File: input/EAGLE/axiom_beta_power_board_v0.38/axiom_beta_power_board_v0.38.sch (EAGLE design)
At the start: 328 parts, among them Q1 NX3008NBKT, U1 PIC16F15325-JQ, U10 AP7312-3333W6-7, U11 AP7312-3333W6-7, U12 AP7312-3333W6-7, U13 AP7312-3333W6-7, U14 PAC1720, U15 PAC1720, U16 PAC1720, U17 PAC1720, U18 PAC1720, U19 PAC1720, U2 TPS82130SIL-GM, U20 PAC1720, U21 PAC1720, U22 PAC1720, U23 PAC1720, U24 PAC1720, U25 PCA9306GM, U26 SC202A, U27 TS3A4751, U28 IP4251CZ16-8-TTL, U29 LM75BGD, U3 TPS82130SIL-GM, U30 PCA9306GM, U31 NCP715, U4 PCA9306GM, U5 PCA9306GM, U6 MCP23018-E/MJ, U7 MCP23018-E/MJ, U8 MCP23018-E/MJ, U9 MCP23018-E/MJ, X1 PICO-SPOX-5

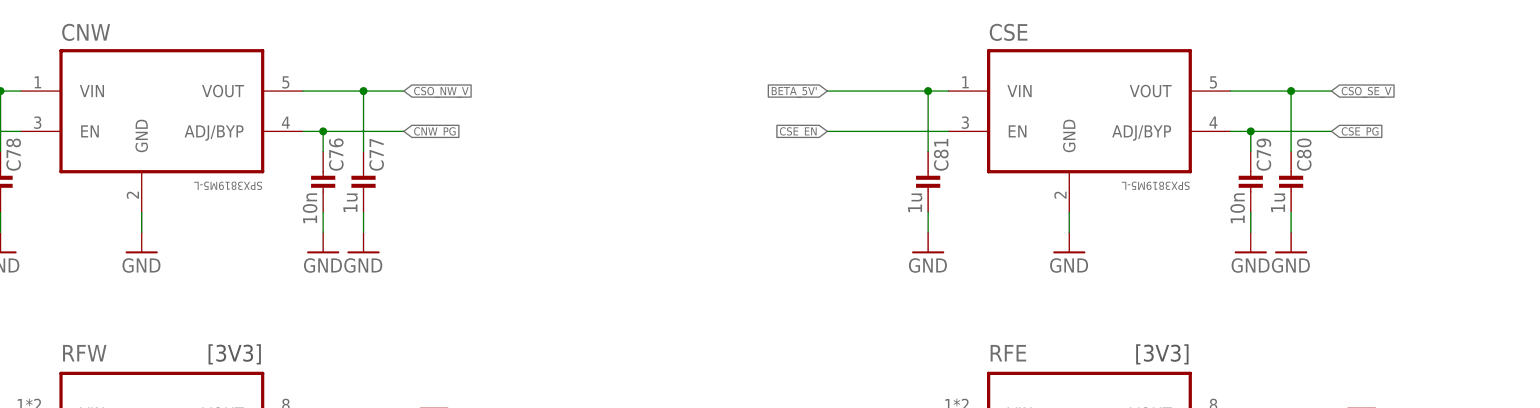
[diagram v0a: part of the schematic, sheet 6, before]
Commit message: MB & PB V0.38 added
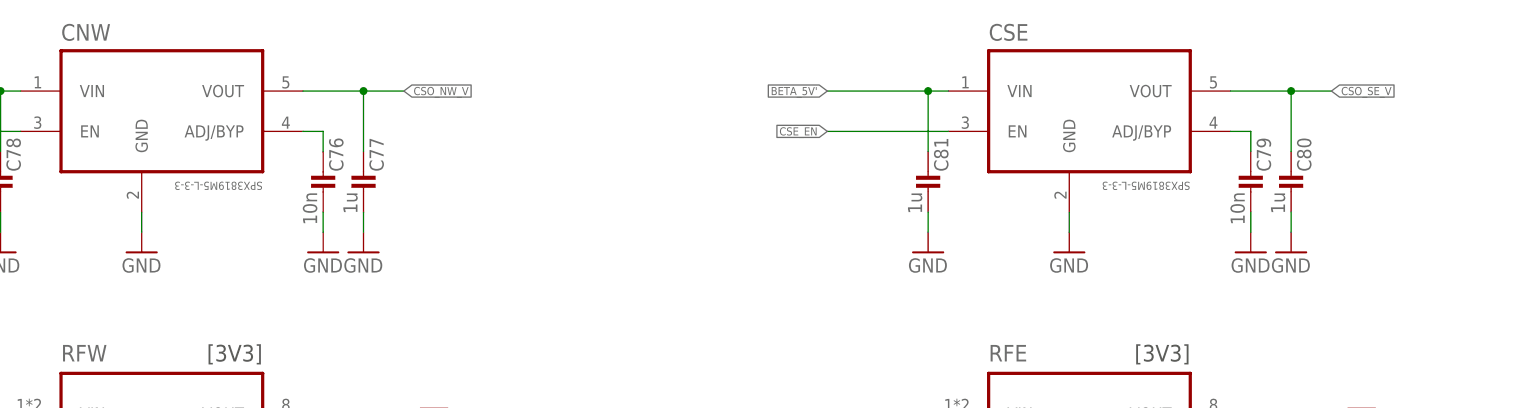
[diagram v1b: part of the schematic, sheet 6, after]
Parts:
- CNW, CSE: value SPX3819M5-L -> SPX3819M5-L-3-3
- JX1B, JX2B: value BERGSTAK-61083 -> BERGSTAK-61083F; device microzed:BERGSTAK-61083 -> microzed:BERGSTAK-61083F
- JX1T, JX2T: value BERGSTAK-61082 -> BERGSTAK-61082F; device microzed:BERGSTAK-61082 -> microzed:BERGSTAK-61082F
- R110: value 523k -> 147k
- R111, R115: value 100k -> 28k
- R114: value 536k -> 147k
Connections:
- new net CNW_BYP: C76.1, CNW.ADJ/BYP
- new net CSE_BYP: C79.1, CSE.ADJ/BYP
- net CNW_PG: no longer C76.1, CNW.ADJ/BYP
- net CSE_PG: no longer C79.1, CSE.ADJ/BYP
